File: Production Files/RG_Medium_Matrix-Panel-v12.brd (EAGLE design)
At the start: 105.7 x 137.2 mm, 91 parts, among them IC1 74LS595D, IC11 74LS595D, IC12 74LS595D, IC2 74LS595D, IC5 74LS595D, IC6 74LS595D, IC8 74LS595D, IC9 74LS595D, U1 AVR_SPI_PRG_6PTH, U2 AVR_SPI_PRG_6PTH, U3 16MHz, U4 16MHz, U5 AVR_SPI_PRG_6PTH, U6 16MHz, U7 AVR_SPI_PRG_6PTH, U8 16MHz

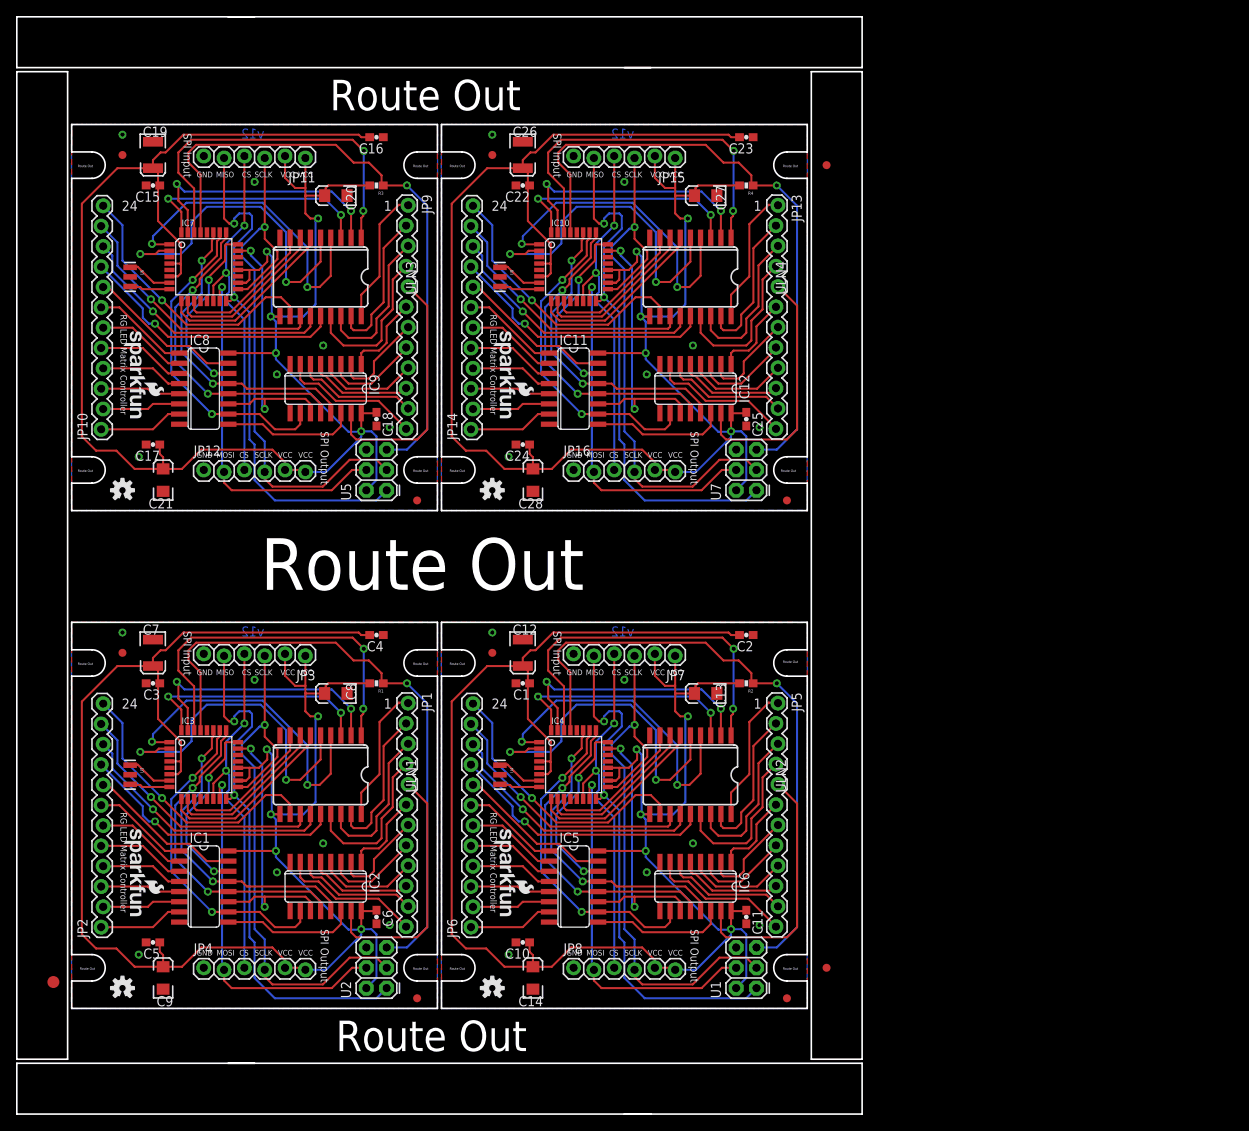
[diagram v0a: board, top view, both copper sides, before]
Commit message: re-created panel v12
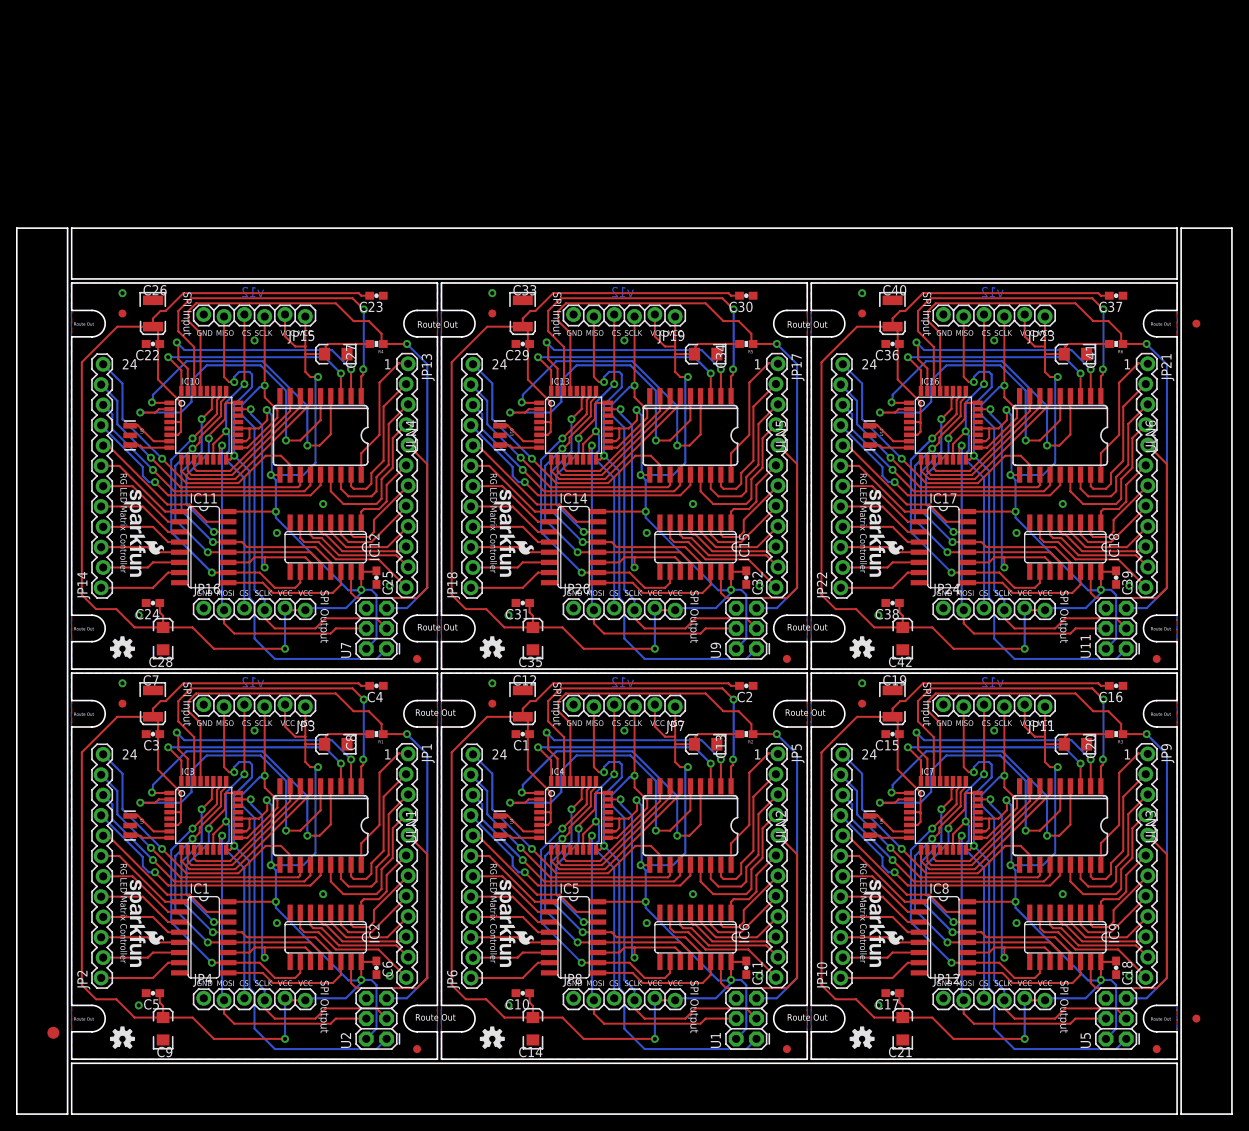
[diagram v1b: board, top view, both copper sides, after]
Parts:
- removed E$5: (no value), SparkFun-Aesthetics:FIDUCIAL-1X2
- added C29, C36: .1uf, SparkFun-Capacitors:0603-CAP
- added C30, C32, C37, C39: 0.1uf, SparkFun-Capacitors:0603-CAP
- added C31, C38: 0.1uF, SparkFun-Capacitors:0603-CAP
- added C33, C40: 47uF, SparkFun:EIA3528
- added C34, C35, C41, C42: 10uF, SparkFun:EIA3216
- added E$6: (no value), SparkFun-Aesthetics:FIDUCIAL-1X2
- added IC13, IC16: (no value), SparkFun-DigitalIC:TQFP32-08
- added IC14, IC15, IC17, IC18: 74LS595D, SparkFun:SO16
- added JP17, JP18, JP21, JP22: M12LOCK, SparkFun-Connectors:1X12_LOCK
- added JP19, JP20, JP23, JP24: (no value), SparkFun-Connectors:1X06_LOCK
- added LOGO10, LOGO12: SFE_LOGO_NAME_FLAME.1_INCH, SparkFun-Aesthetics:SFE_LOGO_NAME_FLAME_.1
- added LOGO11, LOGO9: OSHW-LOGOS, SparkFun-Aesthetics:OSHW-LOGO-S
- added R5, R6: 10K, SparkFun-Resistors:0603-RES
- added U$10, U$11, U$12, U$9: FIDUCIAL1X2, SparkFun:FIDUCIAL-1X2
- added U10, U12: 16MHz, SparkFun:RESONATOR-SMD
- added U11, U9: AVR_SPI_PRG_6PTH, SparkFun-Connectors:2X3
- added ULN5, ULN6: uln2803, SparkFun:SO18L
- moved JP9 115.1 mm to (141.2, 45.0)
- moved C15 115.1 mm to (109.5, 47.5)
- moved C19 115.1 mm to (109.5, 51.3)
- moved C20 115.1 mm to (132.3, 46.2)
- moved C21 115.1 mm to (110.7, 10.7)
- moved IC7 115.1 mm to (115.8, 37.3)
- moved JP11 115.1 mm to (128.5, 50.9)
- moved U$5 115.1 mm to (105.7, 51.3)
- moved C16 115.1 mm to (137.4, 53.5)
- moved C17 115.1 mm to (109.5, 15.1)
- moved C18 115.1 mm to (137.4, 18.3)
- moved IC8 115.1 mm to (115.8, 22.1)
- moved IC9 115.1 mm to (131.1, 22.1)
- moved JP10 115.1 mm to (103.1, 17.0)
- moved LOGO5 115.1 mm to (105.7, 9.40)
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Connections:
- new net CS4: IC13.14, JP19.4, JP20.3
- new net CS5: IC16.14, JP23.4, JP24.3
- new net G33: IC15.15, JP17.5
- new net G34: IC15.1, JP17.6
- new net G35: IC15.2, JP17.7
- new net G36: IC15.3, JP17.8
- new net G37: IC15.4, JP17.9
- new net G38: IC15.5, JP17.10
- new net G39: IC15.6, JP17.11
- new net G40: IC15.7, JP17.12
- new net G41: IC18.15, JP21.5
- new net G42: IC18.1, JP21.6
- new net G43: IC18.2, JP21.7
- new net G44: IC18.3, JP21.8
- new net G45: IC18.4, JP21.9
- new net G46: IC18.5, JP21.10
- new net G47: IC18.6, JP21.11
- new net G48: IC18.7, JP21.12
- new net GND4: C29.2, C30.1, C31.2, C32.2, C33.C, C34.C, C35.C, IC13.21, IC13.3, IC13.5, IC14.8, IC15.8, JP19.6, JP20.1, U10.2, U9.6, ULN5.9
- new net GND5: C36.2, C37.1, C38.2, C39.2, C40.C, C41.C, C42.C, IC16.21, IC16.3, IC16.5, IC17.8, IC18.8, JP23.6, JP24.1, U11.6, U12.2, ULN6.9
- new net MISO4: IC13.16, JP19.5, U9.1
- new net MISO5: IC16.16, JP23.5, U11.1
- new net MOSI4: IC13.15, JP20.2, U9.4
- new net MOSI5: IC16.15, JP24.2, U11.4
- new net N$12: IC14.9, IC15.14
- new net N$13: IC13.7, U10.1
- new net N$14: IC13.8, U10.3
- new net N$15: IC17.9, IC18.14
- new net N$16: IC16.7, U12.1
- new net N$17: IC16.8, U12.3
- new net R33: IC14.15, JP18.8
- new net R34: IC14.1, JP18.7
- new net R35: IC14.2, JP18.6
- new net R36: IC14.3, JP18.5
- new net R37: IC14.4, JP18.4
- new net R38: IC14.5, JP18.3
- new net R39: IC14.6, JP18.2
- new net R40: IC14.7, JP18.1
- new net R41: IC17.15, JP22.8
- new net R42: IC17.1, JP22.7
- new net R43: IC17.2, JP22.6
- new net R44: IC17.3, JP22.5
- new net R45: IC17.4, JP22.4
- new net R46: IC17.5, JP22.3
- new net R47: IC17.6, JP22.2
- new net R48: IC17.7, JP22.1
- new net ROW33: IC13.30, ULN5.1
- new net ROW34: IC13.31, ULN5.2
- new net ROW35: IC13.32, ULN5.3
- new net ROW36: IC13.1, ULN5.4
- new net ROW37: IC13.2, ULN5.5
- new net ROW38: IC13.9, ULN5.6
- new net ROW39: IC13.10, ULN5.7
- new net ROW40: IC13.11, ULN5.8
- new net ROW41: IC16.30, ULN6.1
- new net ROW42: IC16.31, ULN6.2
- new net ROW43: IC16.32, ULN6.3
- new net ROW44: IC16.1, ULN6.4
- new net ROW45: IC16.2, ULN6.5
- new net ROW46: IC16.9, ULN6.6
- new net ROW47: IC16.10, ULN6.7
- new net ROW48: IC16.11, ULN6.8
- new net ROW_33: JP17.1, ULN5.18
- new net ROW_34: JP17.2, ULN5.17
- new net ROW_35: JP17.3, ULN5.16
- new net ROW_36: JP17.4, ULN5.15
- new net ROW_37: JP18.9, ULN5.14
- new net ROW_38: JP18.10, ULN5.13
- new net ROW_39: JP18.11, ULN5.12
- new net ROW_40: JP18.12, ULN5.11
- new net ROW_41: JP21.1, ULN6.18
- new net ROW_42: JP21.2, ULN6.17
- new net ROW_43: JP21.3, ULN6.16
- new net ROW_44: JP21.4, ULN6.15
- new net ROW_45: JP22.9, ULN6.14
- new net ROW_46: JP22.10, ULN6.13
- new net ROW_47: JP22.11, ULN6.12
- new net ROW_48: JP22.12, ULN6.11
- new net RST4: IC13.29, R5.1, U9.5
- new net RST5: IC16.29, R6.1, U11.5
- new net SCK4: IC13.17, JP19.3, JP20.4, U9.3
- new net SCK5: IC16.17, JP23.3, JP24.4, U11.3
- new net SR_CLEAR4: IC13.26, IC14.10, IC15.10
- new net SR_CLEAR5: IC16.26, IC17.10, IC18.10
- new net SR_DATA4: IC13.24, IC14.14
- new net SR_DATA5: IC16.24, IC17.14
- new net SR_EN4: IC13.27, IC14.13, IC15.13
- new net SR_EN5: IC16.27, IC17.13, IC18.13
- new net SR_LATCH4: IC13.25, IC14.12, IC15.12
- new net SR_LATCH5: IC16.25, IC17.12, IC18.12
- new net SR_SCK4: IC13.23, IC14.11, IC15.11
- new net SR_SCK5: IC16.23, IC17.11, IC18.11
- new net VCC4: C29.1, C30.2, C31.1, C32.1, C33.A, C34.A, C35.A, IC13.18, IC13.20, IC13.4, IC13.6, IC14.16, IC15.16, JP19.1, JP19.2, JP20.5, JP20.6, R5.2, U9.2, ULN5.10
- new net VCC5: C36.1, C37.2, C38.1, C39.1, C40.A, C41.A, C42.A, IC16.18, IC16.20, IC16.4, IC16.6, IC17.16, IC18.16, JP23.1, JP23.2, JP24.5, JP24.6, R6.2, U11.2, ULN6.10
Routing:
- net VCC4: track 0.00 -> 235.0 mm, vias 0 -> 6
- net VCC5: track 0.00 -> 235.0 mm, vias 0 -> 6
- net RST5: track 0.00 -> 79.2 mm, vias 0 -> 1
- net RST4: track 0.00 -> 79.2 mm, vias 0 -> 1
- net SCK4: track 0.00 -> 68.3 mm, vias 0 -> 1
- net SCK5: track 0.00 -> 68.3 mm, vias 0 -> 1
- net MISO4: track 0.00 -> 66.6 mm, vias 0 -> 2
- net MISO5: track 0.00 -> 66.6 mm, vias 0 -> 2
- net ROW41: track 0.00 -> 46.2 mm, vias 0 -> 2
- net ROW33: track 0.00 -> 46.2 mm, vias 0 -> 2
- net CS4: track 0.00 -> 43.0 mm, vias 0 -> 2
- net CS5: track 0.00 -> 43.0 mm, vias 0 -> 2
- net MOSI5: track 0.00 -> 42.9 mm, vias 0 -> 1
- net MOSI4: track 0.00 -> 42.9 mm, vias 0 -> 1
- net ROW45: track 0.00 -> 42.0 mm, vias 0 -> 2
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- added copper zone on layer 1, net GND4
- added copper zone on layer 16, net GND4
- added copper zone on layer 1, net GND5
- added copper zone on layer 16, net GND5
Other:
- board size 105.7 x 137.2 mm -> 151.9 x 110.7 mm

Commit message: re-re-created panel v12
this panel has proper spacing for male and female headers
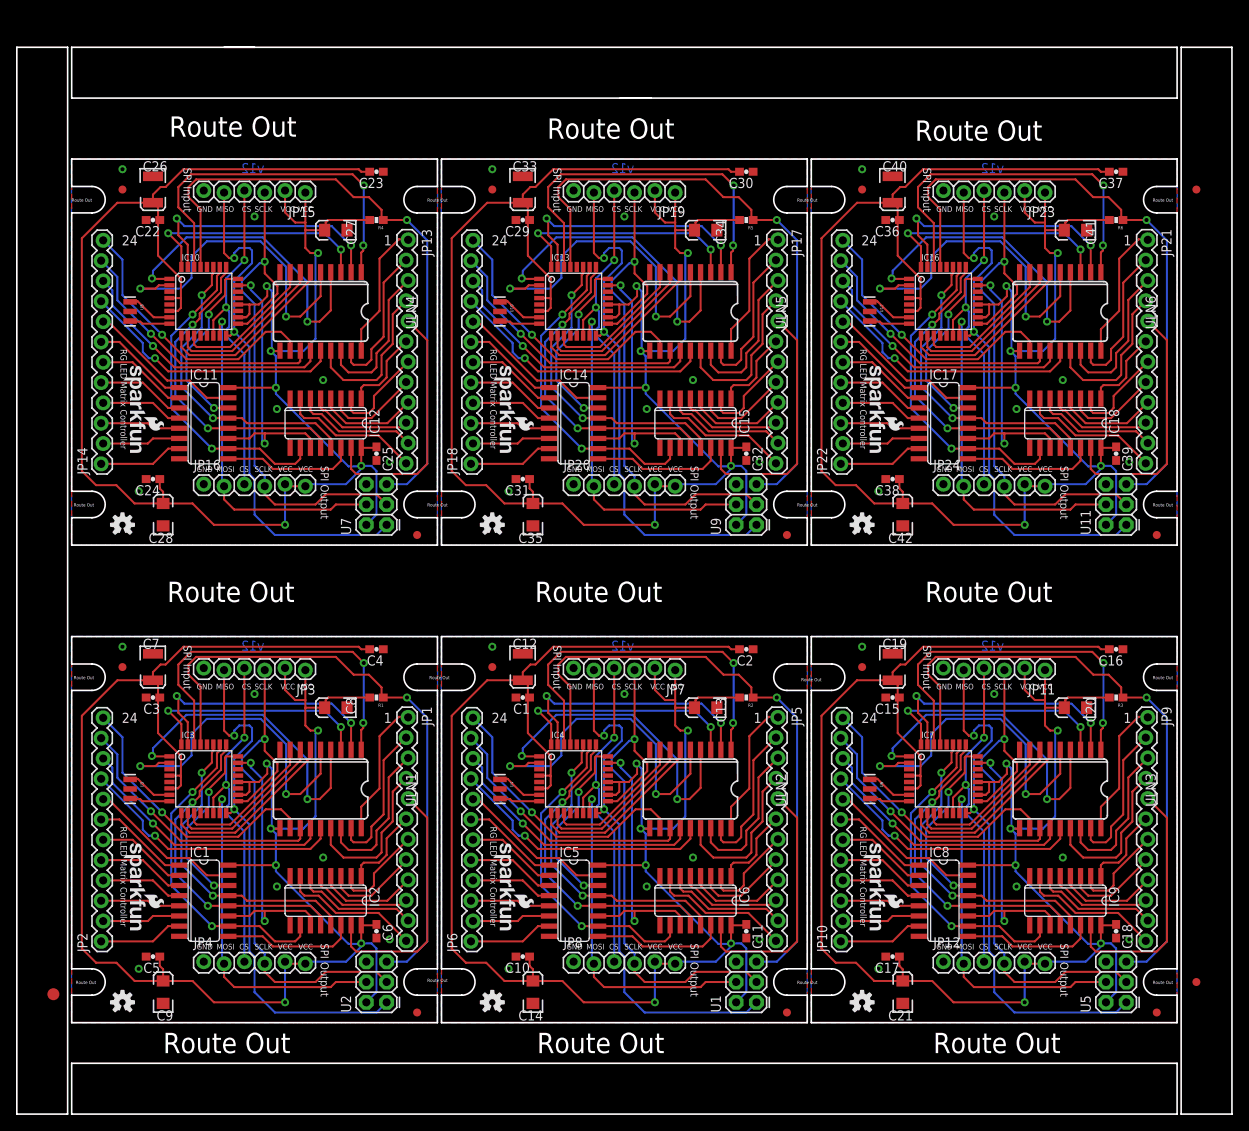
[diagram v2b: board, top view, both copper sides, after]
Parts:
- removed E$6: (no value), SparkFun-Aesthetics:FIDUCIAL-1X2
- added E$3: (no value), SparkFun-Aesthetics:FIDUCIAL-1X2
- moved C28 15.5 mm to (18.3, 74.9)
- moved C35 15.5 mm to (64.5, 74.9)
- moved C42 15.5 mm to (110.7, 74.9)
- moved C22 15.5 mm to (17.0, 111.8)
- moved C23 15.5 mm to (45.0, 117.8)
- moved C24 15.5 mm to (17.0, 79.4)
- moved C25 15.5 mm to (45.0, 82.5)
- moved C26 15.5 mm to (17.0, 115.6)
- moved C27 15.5 mm to (39.9, 110.5)
- moved C29 15.5 mm to (63.2, 111.8)
- moved C30 15.5 mm to (91.2, 117.8)
- moved C31 15.5 mm to (63.2, 79.4)
- moved C32 15.5 mm to (91.2, 82.5)
- moved C33 15.5 mm to (63.2, 115.6)
- moved C34 15.5 mm to (86.1, 110.5)
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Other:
- board size 151.9 x 110.7 mm -> 151.9 x 133.3 mm
- board text added: "R1"
- board text added: "R2"
- board text added: "R3"
- board text added: "R4"
- board text added: "R5"
- board text added: "R6"
- board text added: "R7"
- board text added: "R8"
